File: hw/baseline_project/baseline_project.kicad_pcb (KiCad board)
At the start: 2 copper layers, 115 x 94 mm, 17 parts, among them J101 EXT_3V3, Q101 IRLD024PBF, SW101 UP, SW102 DOWN, SW103 LEFT, SW104 RIGHT, SW105 MODE, U101 EK-TM4C123GXL, U102 ESP8266-01/ESP-01, U103 Adafruit ST7735R

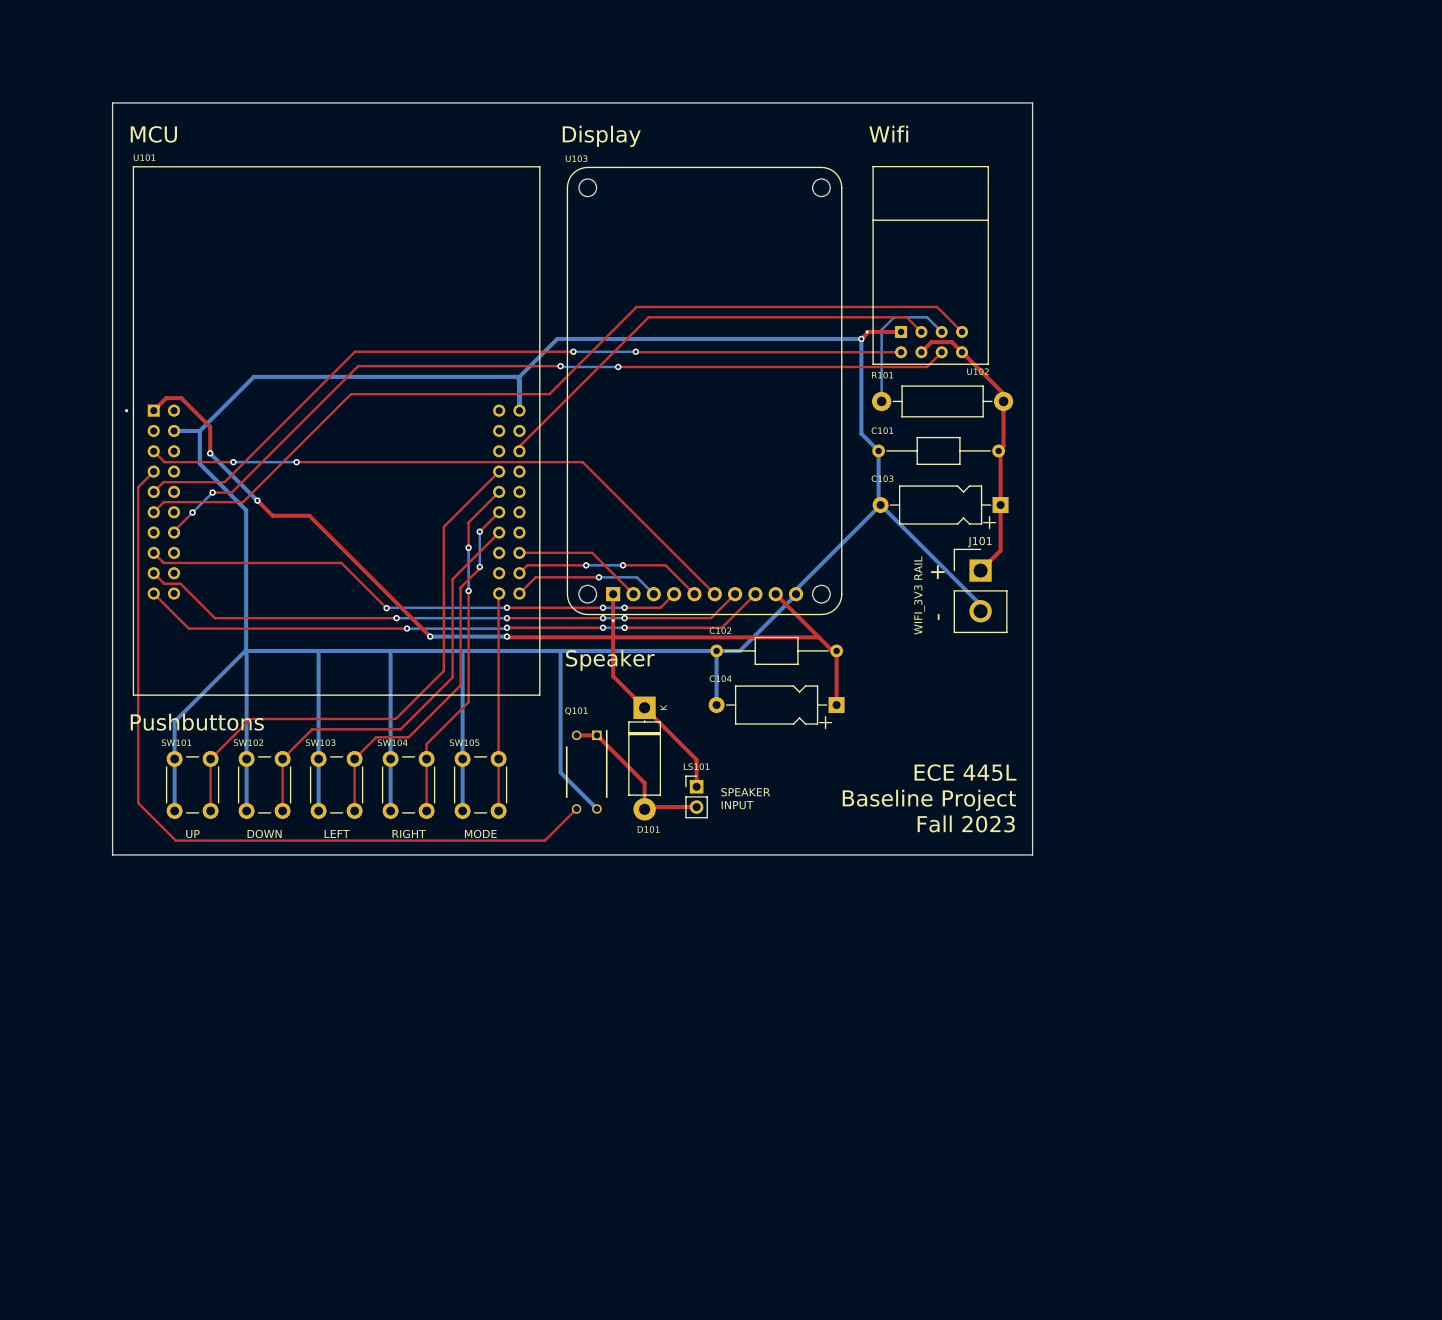
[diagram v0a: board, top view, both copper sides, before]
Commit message: schematic done, pcb design
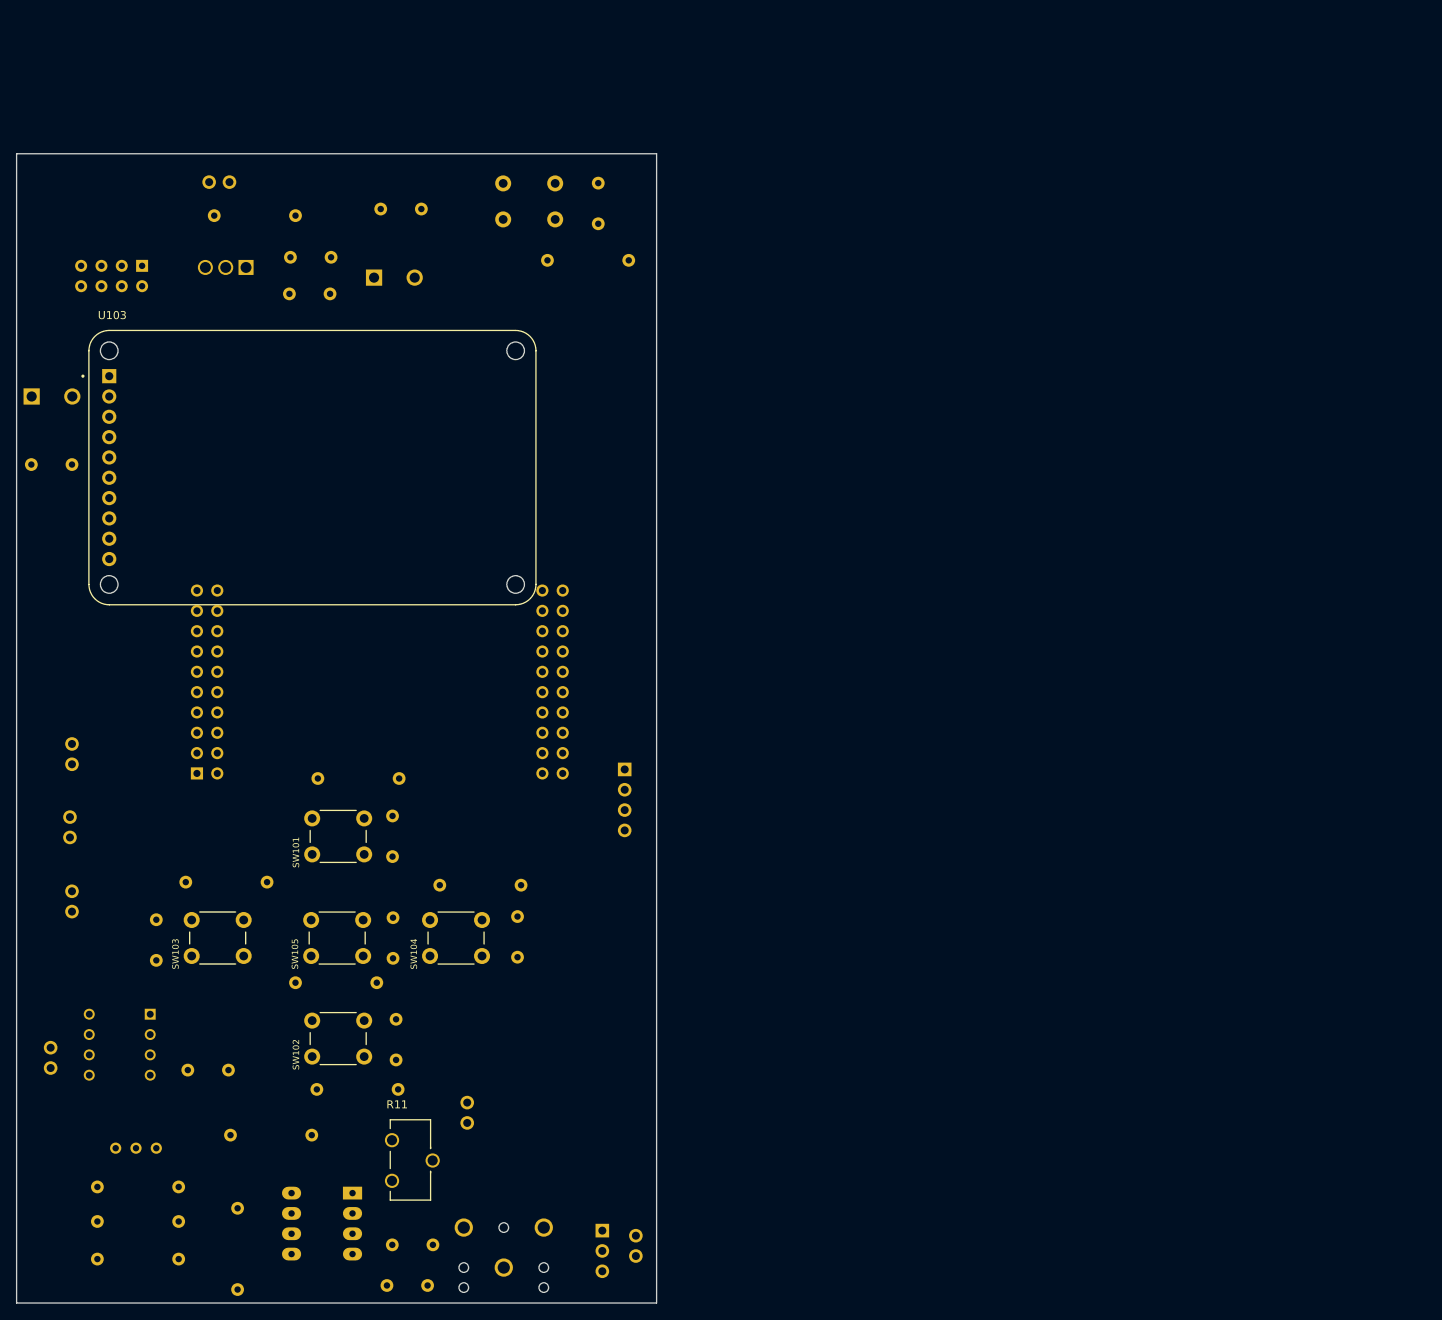
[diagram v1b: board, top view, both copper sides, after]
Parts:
- removed D101: 1V0, Diode_THT:D_5W_P12.70mm_Horizontal
- removed J101: EXT_3V3, Connector_Samtec_HPM_THT:Samtec_HPM-02-01-x-S_Straight_1x02_Pitch5.08mm
- removed LS101: Speaker, Connector_PinHeader_2.54mm:PinHeader_1x02_P2.54mm_Vertical
- removed Q101: IRLD024PBF, footprints:vishay_IRLD024PBF
- added C1: 1uF, ECE445L:C_Axial_200mil, B.Cu at (72.0, 173.7)
- added C10: 0.1uF, ECE445L:C_Axial_200mil, B.Cu at (67.1, 132.8)
- added C11: 0.1uF, ECE445L:C_Axial_200mil, B.Cu at (92.7, 46.1)
- added C2: 0.1uF, ECE445L:C_Axial_200mil, B.Cu at (46.5, 151.9)
- added C3: 4.7uF, ECE445L:C_Axial_200mil, B.Cu at (71.4, 178.8)
- added C4: 4.7uF, ECE445L:C_Axial_200mil, B.Cu at (59.3, 50.3)
- added C5: 4.7uF, ECE445L:C_Axial_200mil, B.Cu at (59.2, 54.9)
- added C6: 0.1uF, ECE445L:C_Axial_200mil, B.Cu at (67.0, 120.1)
- added C7: 0.1uF, ECE445L:C_Axial_200mil, B.Cu at (67.4, 145.5)
- added C8: 0.1uF, ECE445L:C_Axial_200mil, B.Cu at (37.5, 133.1)
- added C9: 0.1uF, ECE445L:C_Axial_200mil, B.Cu at (82.6, 132.7)
- added IC1: LM4041CILPR, ECE445L:ti_LM4041CILPR, B.Cu at (34.9, 161.7)
- added J1: AudioJack, ECE445L:Jack_3.5mm_CUI_SJ1-3523N_Horizontal, B.Cu at (80.9, 176.6)
- added J2: Header_4, ECE445L:PinHeader_1x04_P2.54mm_Vertical, B.Cu at (96.0, 114.3)
- added JP1: Jumper_3_Open, ECE445L:PinHeader_1x03_P2.54mm_Vertical, B.Cu at (93.2, 172.0)
- added R1: 20k, Resistor_THT:R_Axial_DIN0207_L6.3mm_D2.5mm_P10.16mm_Horizontal, B.Cu at (56.9, 160.0)
- added R10: 10k, Resistor_THT:R_Axial_DIN0207_L6.3mm_D2.5mm_P10.16mm_Horizontal, B.Cu at (65.0, 141.0)
- added R11: 10k, ECE445L:Potentiometer, F.Cu at (68.2, 163.2)
- added R12: 10k, Resistor_THT:R_Axial_DIN0207_L6.3mm_D2.5mm_P10.16mm_Horizontal, B.Cu at (96.5, 50.7)
- added R2: 10k, Resistor_THT:R_Axial_DIN0207_L6.3mm_D2.5mm_P10.16mm_Horizontal, B.Cu at (47.6, 179.3)
- added R3: 2k, Resistor_THT:R_Axial_DIN0207_L6.3mm_D2.5mm_P10.16mm_Horizontal, B.Cu at (40.3, 166.5)
- added R4: 47k, Resistor_THT:R_Axial_DIN0207_L6.3mm_D2.5mm_P10.16mm_Horizontal, B.Cu at (40.3, 170.8)
- added R5: 10k, Resistor_THT:R_Axial_DIN0207_L6.3mm_D2.5mm_P10.16mm_Horizontal, B.Cu at (40.3, 175.5)
- added R6: 10k, Resistor_THT:R_Axial_DIN0207_L6.3mm_D2.5mm_P10.16mm_Horizontal, B.Cu at (67.8, 115.4)
- added R7: 10k, Resistor_THT:R_Axial_DIN0207_L6.3mm_D2.5mm_P10.16mm_Horizontal, B.Cu at (67.7, 154.3)
- added R8: 10k, Resistor_THT:R_Axial_DIN0207_L6.3mm_D2.5mm_P10.16mm_Horizontal, B.Cu at (51.3, 128.4)
- added R9: 10k, Resistor_THT:R_Axial_DIN0207_L6.3mm_D2.5mm_P10.16mm_Horizontal, B.Cu at (83.1, 128.8)
- added SW1: RESET, Button_Switch_THT:SW_PUSH_6mm, B.Cu at (87.3, 41.1)
- added TP1: TP, ECE445L:Testpoint_1x02_P2.54mm, B.Cu at (97.4, 172.6)
- added TP2: TP, ECE445L:Testpoint_1x02_P2.54mm, B.Cu at (24.3, 149.1)
- added TP3: TP, ECE445L:Testpoint_1x02_P2.54mm, B.Cu at (76.3, 156.0)
- added TP4: TP, ECE445L:Testpoint_1x02_P2.54mm, B.Cu at (26.9, 111.1)
- added TP5: TP, ECE445L:Testpoint_1x02_P2.54mm, B.Cu at (26.7, 120.3)
- added TP6: TP, ECE445L:Testpoint_1x02_P2.54mm, B.Cu at (26.9, 129.5)
- added TP7: TP, ECE445L:Testpoint_1x02_P2.54mm, B.Cu at (44.1, 40.9)
- added U1: TLV5616CP, ECE445L:ul_TLV5616CP, B.Cu at (29.1, 152.5)
- added U3: LM2937xMP, ECE445L:LM2937, B.Cu at (48.7, 51.6)
- added U4: MCP34119P, ECE445L:DIP-8_W7.62mm_LongPads, B.Cu at (62.0, 167.3)
- C101, C102: footprint Capacitor_THT:C_Axial_L5.1mm_D3.1mm_P15.00mm_Horizontal -> ECE445L:C_Axial_200mil; moved to B.Cu
- C103, C104: footprint Capacitor_THT:CP_Axial_L10.0mm_D4.5mm_P15.00mm_Horizontal -> ECE445L:CP_Radial_Tantal200mil; moved to B.Cu
- R101: footprint Resistor_THT:R_Axial_DIN0411_L9.9mm_D3.6mm_P15.24mm_Horizontal -> Resistor_THT:R_Axial_DIN0207_L6.3mm_D2.5mm_P10.16mm_Horizontal; moved to B.Cu
- U101: footprint footprints:ti_EKTM4C123GXL -> ECE445L:ti_EKTM4C123GXL; moved to B.Cu
- U102: footprint footprints:ai_thinker_ESP8266_01 -> ECE445L:ai_thinker_ESP8266_01; moved to B.Cu
- U103: footprint footprints:adafruit_st7735r -> ECE445L:adafruit_st7735r
- moved C104 107.8 mm to (21.9, 67.7), turned to 0 degrees
- moved C102 103.3 mm to (21.8, 76.2), turned to 0 degrees
- moved U102 102.8 mm to (31.9, 43.1), turned to 180 degrees
- moved R101 101.4 mm to (44.7, 45.1), turned to 0 degrees
- moved C103 83.3 mm to (64.7, 52.8), turned to 0 degrees
- moved C101 82.9 mm to (65.5, 44.3), turned to 0 degrees
- moved U103 49.9 mm to (57.0, 76.6), turned to 0 degrees
- moved U101 40.6 mm to (65.4, 112.3)
- moved SW102 34.0 mm to (63.4, 150.2), turned to 180 degrees
- moved SW101 24.3 mm to (63.4, 124.9), turned to 180 degrees
- moved SW105 22.0 mm to (63.3, 137.6), turned to 180 degrees
- moved SW104 21.4 mm to (78.2, 137.6), turned to 180 degrees
- moved SW103 20.4 mm to (48.4, 137.6), turned to 180 degrees
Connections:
- SW101 pad 1: GND -> +3V3
- SW102 pad 1: GND -> +3V3
- SW103 pad 1: GND -> +3V3
- SW104 pad 1: GND -> +3V3
- U101 pad J1_4: /SPEAKER_GATE -> unconnected-(U101-PB1-PadJ1_4)
- U101 pad J2_5: unconnected-(U101-~{TARGETRST}-PadJ2_5) -> /RST
- U101 pad J3_10: unconnected-(U101-PF1-PadJ3_10) -> /RED_LED
- U101 pad J3_3: unconnected-(U101-PD0-PadJ3_3) -> /SS1_SCLK
- U101 pad J3_4: unconnected-(U101-PD1-PadJ3_4) -> /SS1_FS
- U101 pad J3_6: unconnected-(U101-PD3-PadJ3_6) -> /SSI1_TX
- U101 pad J4_1: unconnected-(U101-PF2-PadJ4_1) -> /BLUE_LED
- U101 pad J4_2: unconnected-(U101-PF3-PadJ4_2) -> /GREEN_LED
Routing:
- net GND: track 392.9 -> 0.00 mm, vias 1 -> 0
- net +3V3: track 143.8 -> 0.00 mm, vias 4 -> 0
- net /WIFI_RXD: track 113.0 -> 0.00 mm
- net /~{WIFI_RST}: track 105.5 -> 0.00 mm, vias 4 -> 0
- net /WIFI_TXD: track 100.7 -> 0.00 mm, vias 2 -> 0
- net /SPEAKER_GATE: track 100.6 -> 0.00 mm
- net /TFT_RST: track 78.8 -> 0.00 mm, vias 4 -> 0
- net /SDC_CS: track 77.5 -> 0.00 mm, vias 2 -> 0
- net /TFT_D/C: track 76.2 -> 0.00 mm, vias 4 -> 0
- net /TFT_MOSI: track 68.6 -> 0.00 mm, vias 4 -> 0
- net /SW_UP: track 68.0 -> 0.00 mm
- net /WIFI_IO2: track 58.3 -> 0.00 mm
- net /SW_DOWN: track 52.5 -> 0.00 mm
- net /SW_LEFT: track 47.2 -> 0.00 mm, vias 2 -> 0
- net /SW_RIGHT: track 43.6 -> 0.00 mm, vias 2 -> 0
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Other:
- board size 115 x 94 mm -> 80 x 143.7 mm
- board text removed: "+"
- board text removed: "-"
- board text removed: "DOWN"
- board text removed: "Display"
- board text removed: "ECE 445L Baseline Project Fall 2023"
- board text removed: "LEFT"
- board text removed: "MCU"
- board text removed: "MODE"
- board text removed: "Pushbuttons"
- board text removed: "RIGHT"
- board text removed: "SPEAKER INPUT"
- board text removed: "Speaker"
- board text removed: "UP"
- board text removed: "WIFI_3V3 RAIL"
- board text removed: "Wifi"

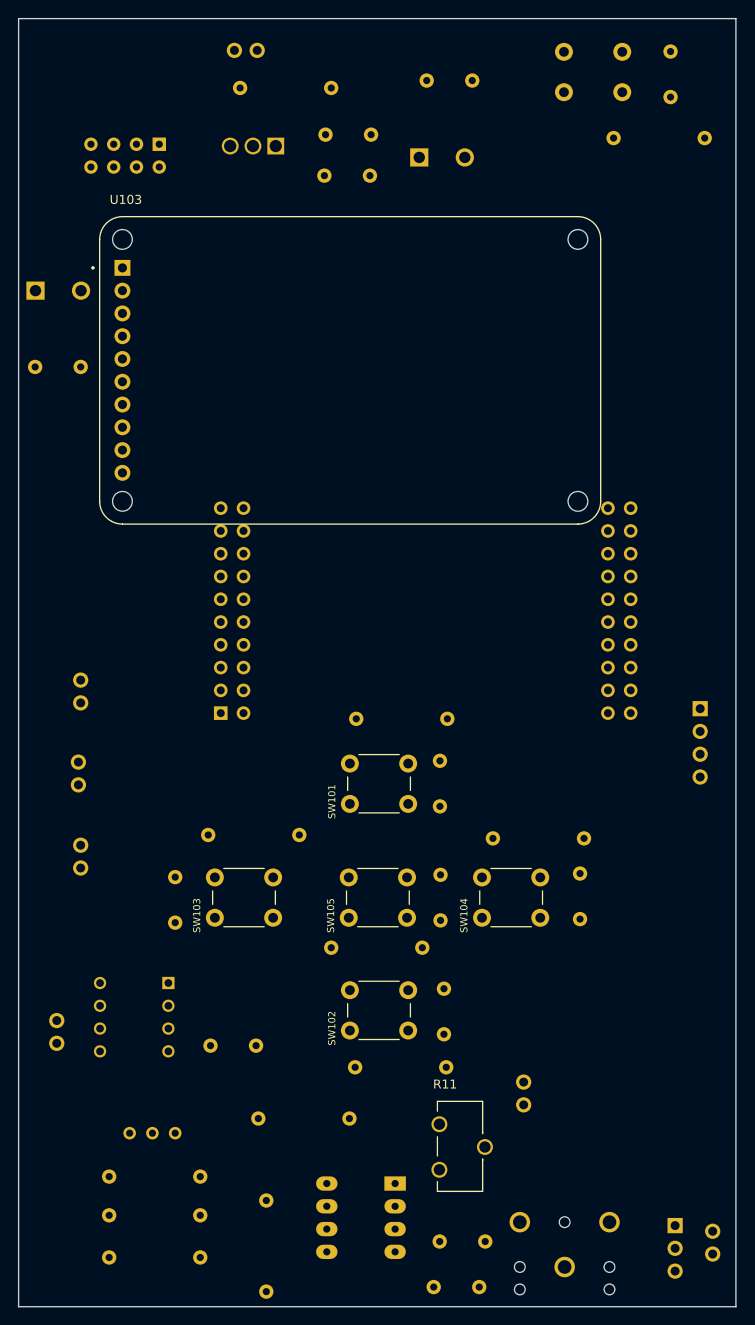
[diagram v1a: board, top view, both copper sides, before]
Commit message: placement ST7735 board
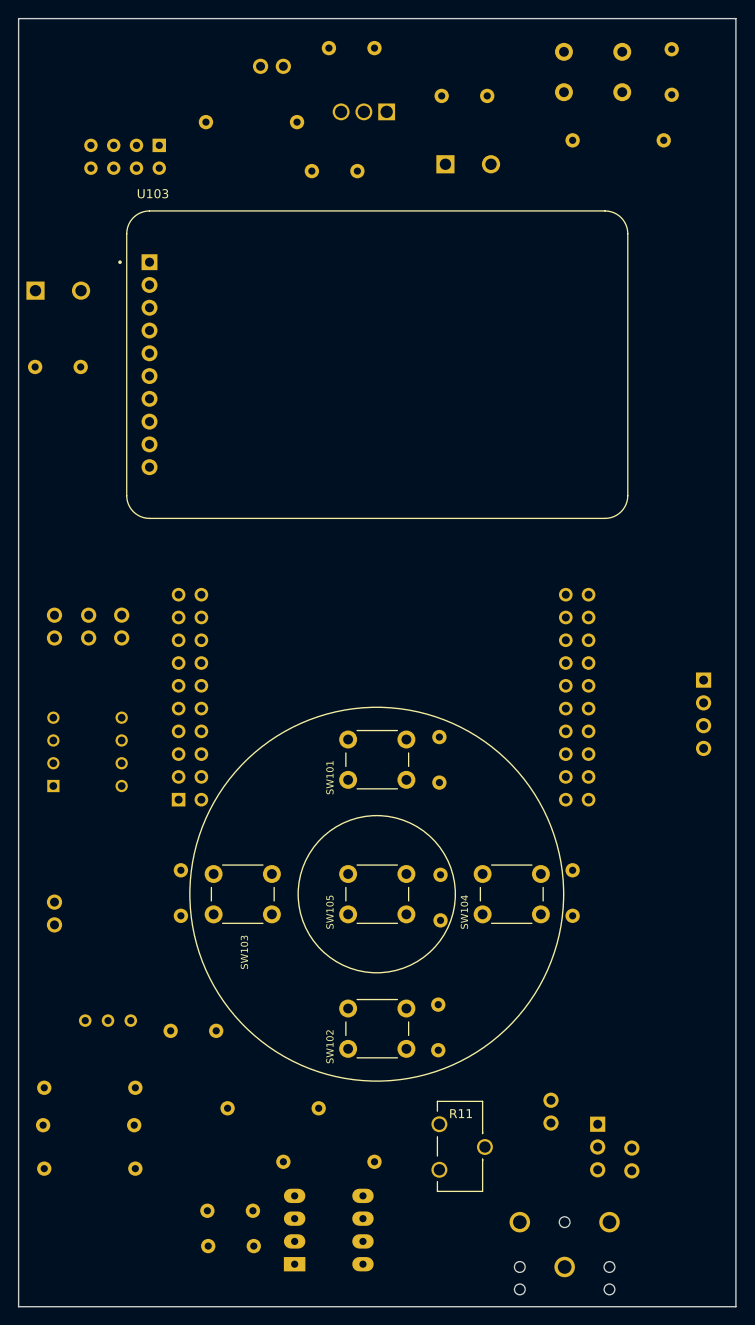
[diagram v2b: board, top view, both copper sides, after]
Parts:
- removed R10, R6, R7, R8, R9: 10k, Resistor_THT:R_Axial_DIN0207_L6.3mm_D2.5mm_P10.16mm_Horizontal
- moved U1 37.3 mm to (31.5, 115.3), turned to 0 degrees
- moved C1 26.1 mm to (46.1, 170.3)
- moved TP6 25.7 mm to (27.8, 103.9)
- moved C3 25.6 mm to (46.2, 174.2)
- moved R4 20.2 mm to (22.7, 160.8), turned to 0 degrees
- moved TP5 16.6 mm to (24.0, 103.9)
- moved R2 14.6 mm to (49.5, 164.8), turned to 0 degrees
- moved U4 14.4 mm to (50.8, 176.3), turned to 0 degrees
- moved JP1 14.2 mm to (84.6, 160.7)
- moved R1 13.6 mm to (43.3, 158.9), turned to 0 degrees
- moved IC1 13.5 mm to (30.0, 149.1)
- moved TP2 13.2 mm to (24.0, 135.9)
- moved U3 12.9 mm to (61.0, 47.8)
- moved TP1 12.9 mm to (88.4, 163.3)
- moved R3 12.3 mm to (33.0, 156.6)
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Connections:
- C6 pad 2: +3V3 -> GND
- C7 pad 2: +3V3 -> GND
- C8 pad 2: +3V3 -> GND
- C9 pad 2: +3V3 -> GND
- J1 pad S: Net-(J1-sleeve) -> GND
- SW101 pad 1: +3V3 -> GND
- SW102 pad 1: +3V3 -> GND
- SW103 pad 1: +3V3 -> GND
- SW104 pad 1: +3V3 -> GND
- U4 pad 8: Net-(J1-sleeve) -> unconnected-(U4-VO2-Pad8)
